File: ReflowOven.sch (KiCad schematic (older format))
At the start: 0 parts

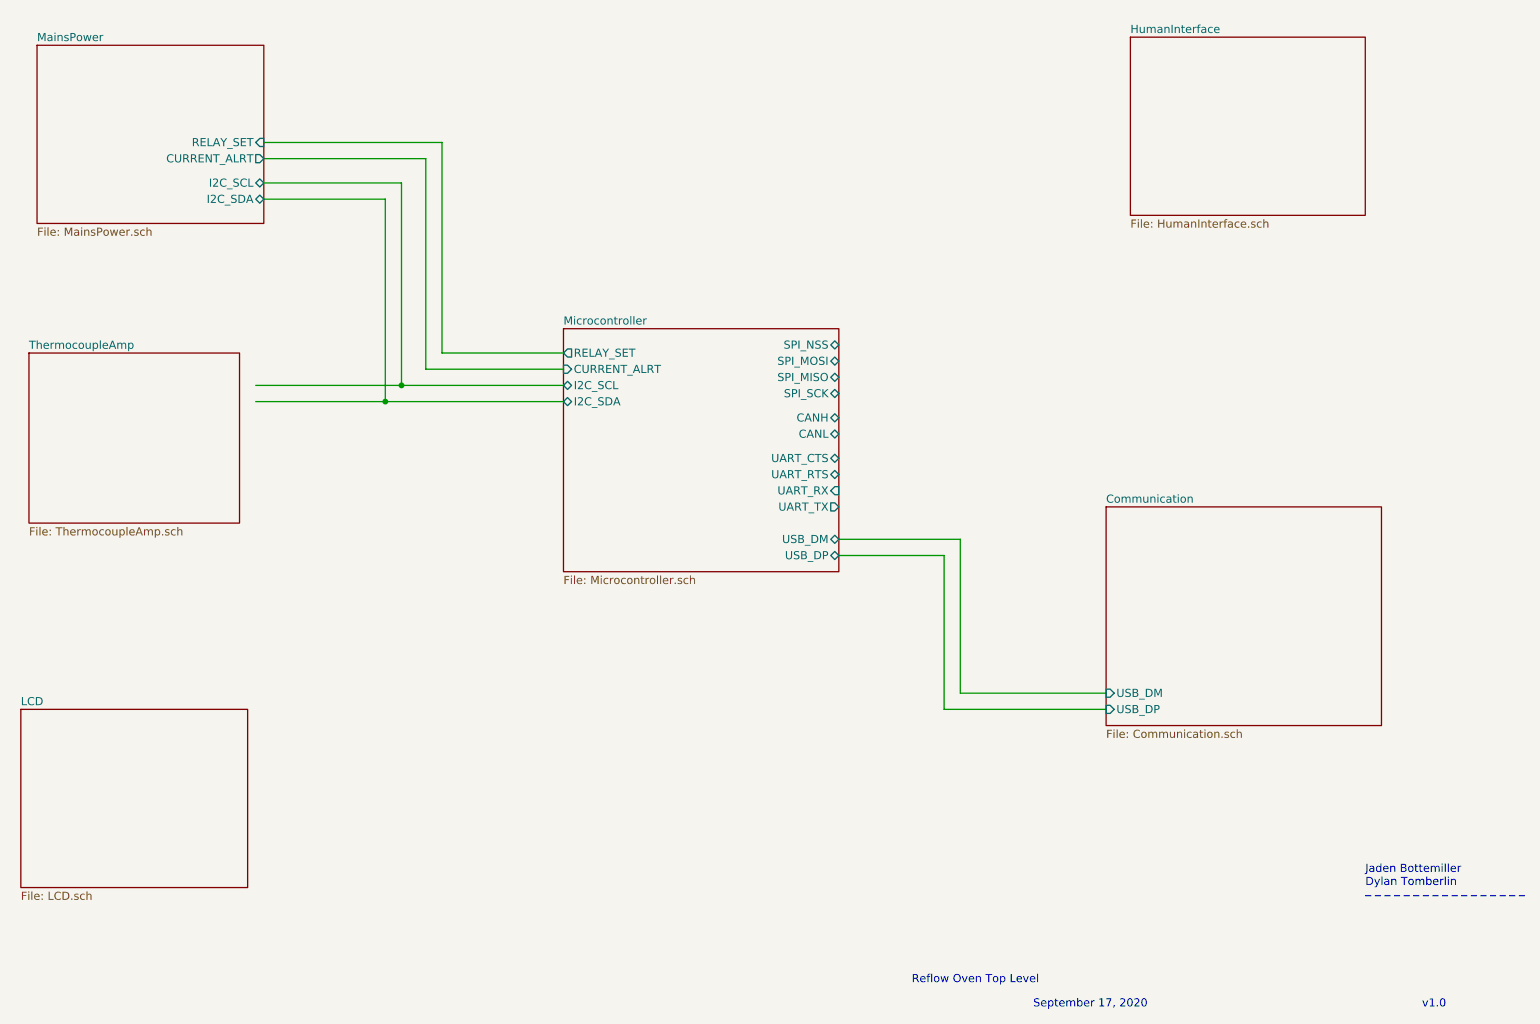
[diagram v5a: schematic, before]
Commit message: Added display driver for 7 segment
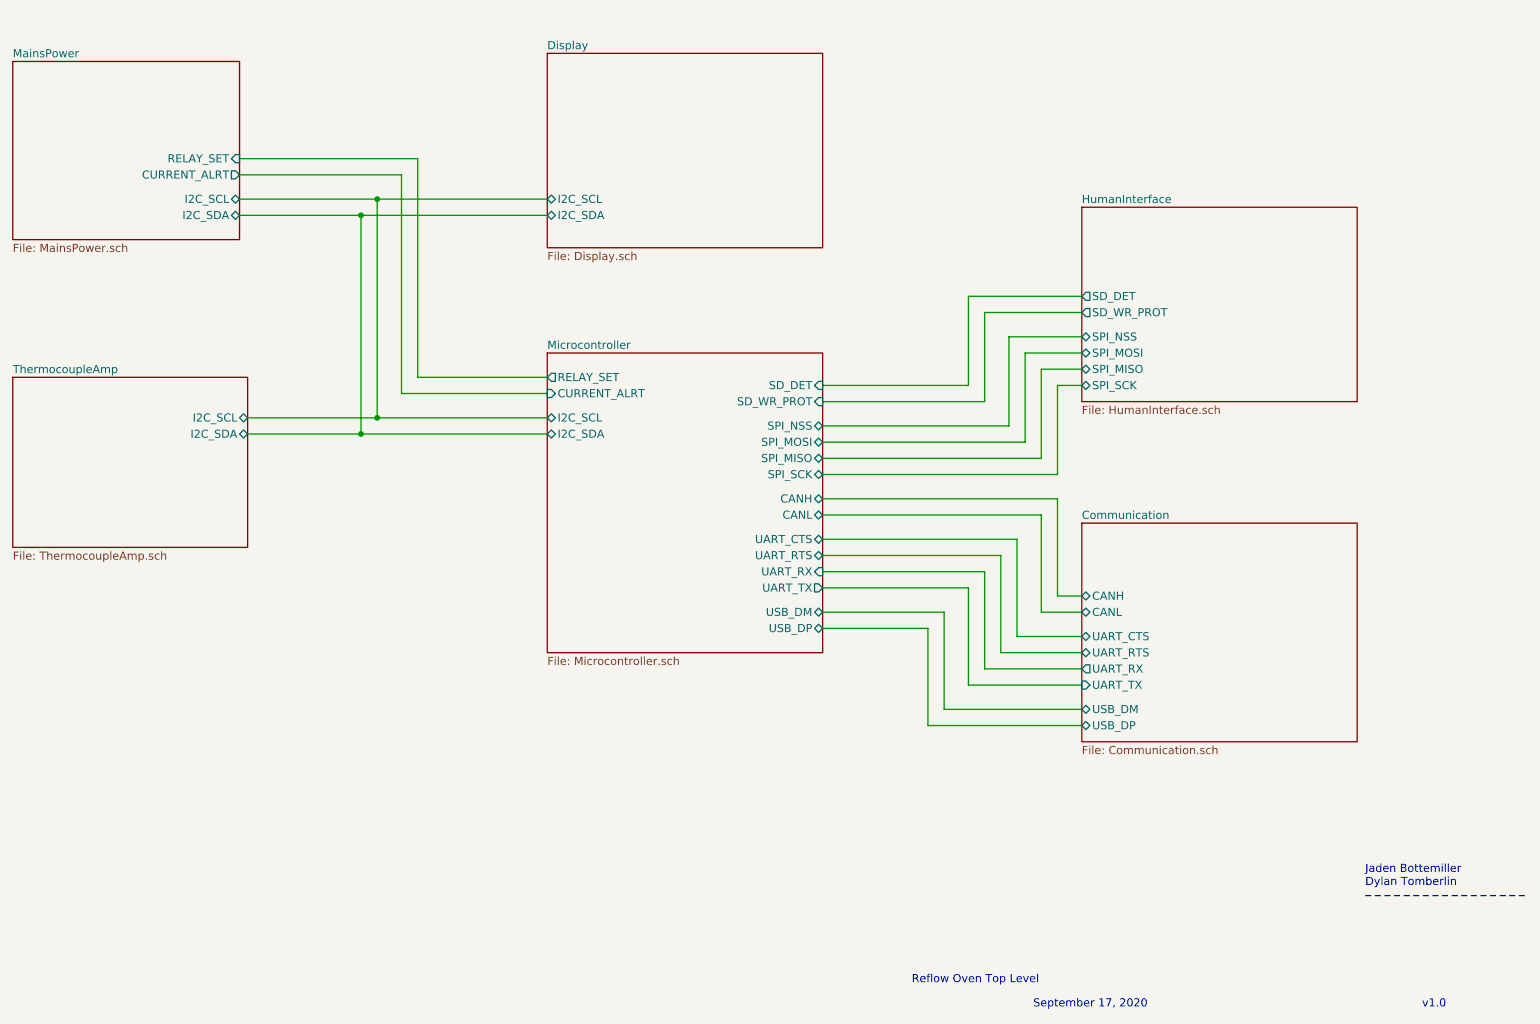
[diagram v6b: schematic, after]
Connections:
- wire segments 20 -> 58
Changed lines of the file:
@@
 	10200 6950 11200 6950
 $Sheet
-S 5250 3450 1700 1500
+S 5150 3600 1700 1850
 U 5F6415F0
 F0 "Microcontroller" 50
 F1 "Microcontroller.sch" 50
-F2 "RELAY_SET" O L 5250 3600 50
-F3 "CURRENT_ALRT" I L 5250 3700 50
-F4 "I2C_SCL" B L 5250 3800 50
-F5 "I2C_SDA" B L 5250 3900 50
-F6 "USB_DP" B R 6950 4850 50
-F7 "USB_DM" B R 6950 4750 50
-F8 "UART_TX" O R 6950 4550 50
-F9 "UART_RX" I R 6950 4450 50
-F10 "UART_RTS" B R 6950 4350 50
-F11 "UART_CTS" B R 6950 4250 50
-F12 "SPI_SCK" B R 6950 3850 50
-F13 "SPI_MISO" B R 6950 3750 50
-F14 "SPI_MOSI" B R 6950 3650 50
-F15 "SPI_NSS" B R 6950 3550 50
-F16 "CANL" B R 6950 4100 50
-F17 "CANH" B R 6950 4000 50
+F2 "RELAY_SET" O L 5150 3750 50
+F3 "CURRENT_ALRT" I L 5150 3850 50
+F4 "I2C_SCL" B L 5150 4000 50
+F5 "I2C_SDA" B L 5150 4100 50
+F6 "USB_DP" B R 6850 5300 50
+F7 "USB_DM" B R 6850 5200 50
+F8 "UART_TX" O R 6850 5050 50
+F9 "UART_RX" I R 6850 4950 50
+F10 "UART_RTS" B R 6850 4850 50
+F11 "UART_CTS" B R 6850 4750 50
+F12 "SPI_SCK" B R 6850 4350 50
+F13 "SPI_MISO" B R 6850 4250 50
+F14 "SPI_MOSI" B R 6850 4150 50
+F15 "SPI_NSS" B R 6850 4050 50
+F16 "CANL" B R 6850 4600 50
+F17 "CANH" B R 6850 4500 50
+F18 "SD_WR_PROT" I R 6850 3900 50
+F19 "SD_DET" I R 6850 3800 50
 $EndSheet
 $Sheet
-S 1900 5800 1400 1100
+S 5150 1750 1700 1200
 U 5F6416B8
-F0 "LCD" 50
-F1 "LCD.sch" 50
+F0 "Display" 50
+F1 "Display.sch" 50
+F2 "I2C_SCL" B L 5150 2650 50
+F3 "I2C_SDA" B L 5150 2750 50
 $EndSheet
 $Sheet
-S 8750 1650 1450 1100
+S 8450 2700 1700 1200
 U 5F641779
 F0 "HumanInterface" 50
 F1 "HumanInterface.sch" 50
+F2 "SPI_SCK" B L 8450 3800 50
+F3 "SPI_MISO" B L 8450 3700 50
+F4 "SPI_MOSI" B L 8450 3600 50
+F5 "SPI_NSS" B L 8450 3500 50
+F6 "SD_DET" O L 8450 3250 50
+F7 "SD_WR_PROT" O L 8450 3350 50
 $EndSheet
 $Sheet
-S 8600 4550 1700 1350
+S 8450 4650 1700 1350
 U 5F641C10
 F0 "Communication" 50
 F1 "Communication.sch" 50
-F2 "USB_DP" I L 8600 5800 50
-F3 "USB_DM" I L 8600 5700 50
+F2 "USB_DP" B L 8450 5900 50
+F3 "USB_DM" B L 8450 5800 50
+F4 "UART_TX" I L 8450 5650 50
+F5 "UART_RX" O L 8450 5550 50
+F6 "UART_RTS" B L 8450 5450 50
+F7 "UART_CTS" B L 8450 5350 50
+F8 "CANH" B L 8450 5100 50
+F9 "CANL" B L 8450 5200 50
 $EndSheet
 Wire Wire Line
-	4500 3600 4500 2300
+	4350 3750 4350 2400
 Wire Wire Line
-	4500 2300 3400 2300
+	4350 2400 3250 2400
 Wire Wire Line
-	4500 3600 5250 3600
+	4350 3750 5150 3750
 $Sheet
-S 2000 1700 1400 1100
+S 1850 1800 1400 1100
 U 5F641519
 F0 "MainsPower" 50
 F1 "MainsPower.sch" 50
-F2 "RELAY_SET" I R 3400 2300 50
-F3 "CURRENT_ALRT" O R 3400 2400 50
-F4 "I2C_SCL" B R 3400 2550 50
-F5 "I2C_SDA" B R 3400 2650 50
+F2 "RELAY_SET" I R 3250 2400 50
+F3 "CURRENT_ALRT" O R 3250 2500 50
+F4 "I2C_SCL" B R 3250 2650 50
+F5 "I2C_SDA" B R 3250 2750 50
 $EndSheet
 Wire Wire Line
-	5250 3700 4400 3700
+	5150 3850 4250 3850
 Wire Wire Line
-	4400 3700 4400 2400
+	4250 3850 4250 2500
 Wire Wire Line
-	4400 2400 3400 2400
+	4250 2500 3250 2500
 Wire Wire Line
-	3400 2550 4250 2550
+	3250 2650 4100 2650
 Wire Wire Line
-	4250 2550 4250 3800
+	4100 2650 4100 4000
 Wire Wire Line
-	4250 3800 5250 3800
+	4100 4000 5150 4000
 Wire Wire Line
-	4150 3900 4150 2650
+	4000 4100 4000 2750
 Wire Wire Line
-	4150 2650 3400 2650
+	4000 2750 3250 2750
 Wire Wire Line
-	4150 3900 5250 3900
+	4000 4100 5150 4100
 $Sheet
-S 1950 3600 1300 1050
+S 1850 3750 1450 1050
 U 5F67E1E1
 F0 "ThermocoupleAmp" 50
 F1 "ThermocoupleAmp.sch" 50
+F2 "I2C_SCL" B R 3300 4000 50
+F3 "I2C_SDA" B R 3300 4100 50
 $EndSheet
+Connection ~ 4100 4000
+Connection ~ 4000 4100
 Wire Wire Line
-	4250 3800 3350 3800
-Connection ~ 4250 3800
+	6850 5300 7500 5300
 Wire Wire Line
-	4150 3900 3350 3900
-Connection ~ 4150 3900
+	7500 5300 7500 5900
 Wire Wire Line
-	6950 4850 7600 4850
+	7500 5900 8450 5900
 Wire Wire Line
-	7600 4850 7600 5800
+	8450 5800 7600 5800
 Wire Wire Line
-	7600 5800 8600 5800
+	7600 5800 7600 5200
 Wire Wire Line
-	8600 5700 7700 5700
+	7600 5200 6850 5200
 Wire Wire Line
-	7700 5700 7700 4750
+	8450 5650 7750 5650
 Wire Wire Line
-	7700 4750 6950 4750
+	7750 5650 7750 5050
+Wire Wire Line
+	7750 5050 6850 5050
+Wire Wire Line
+	6850 4950 7850 4950
+Wire Wire Line
+	7850 4950 7850 5550
+Wire Wire Line
+	7850 5550 8450 5550
+Wire Wire Line
+	8450 5450 7950 5450
+Wire Wire Line
+	7950 5450 7950 4850
+Wire Wire Line
+	7950 4850 6850 4850
+Wire Wire Line
+	6850 4750 8050 4750
+Wire Wire Line
+	8050 4750 8050 5350
+Wire Wire Line
+	8050 5350 8450 5350
+Wire Wire Line
+	8450 5200 8200 5200
+Wire Wire Line
+	8200 5200 8200 4600
+Wire Wire Line
+	8200 4600 6850 4600
+Wire Wire Line
+	6850 4500 8300 4500
+Wire Wire Line
+	8300 4500 8300 5100
+Wire Wire Line
+	8300 5100 8450 5100
+Wire Wire Line
+	8300 4350 8300 3800
+Wire Wire Line
+	8300 3800 8450 3800
+Wire Wire Line
+	6850 4350 8300 4350
+Wire Wire Line
+	8200 3700 8200 4250
+Wire Wire Line
+	8200 4250 6850 4250
+Wire Wire Line
+	8200 3700 8450 3700
+Wire Wire Line
+	8450 3600 8100 3600
+Wire Wire Line
+	8100 3600 8100 4150
+Wire Wire Line
+	8100 4150 6850 4150
+Wire Wire Line
+	6850 4050 8000 4050
+Wire Wire Line
+	8000 4050 8000 3500
+Wire Wire Line
+	8000 3500 8450 3500
+Wire Wire Line
+	7850 3350 7850 3900
+Wire Wire Line
+	7850 3900 6850 3900
+Wire Wire Line
+	7850 3350 8450 3350
+Wire Wire Line
+	6850 3800 7750 3800
+Wire Wire Line
+	7750 3800 7750 3250
+Wire Wire Line
+	7750 3250 8450 3250
+Wire Wire Line
+	3300 4100 4000 4100
+Wire Wire Line
+	3300 4000 4100 4000
+Wire Wire Line
+	4100 2650 5150 2650
+Connection ~ 4100 2650
+Wire Wire Line
+	4000 2750 5150 2750
+Connection ~ 4000 2750
 $EndSCHEMATC

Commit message: Done with preliminary schematic. Needs review
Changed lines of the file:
@@
 	10200 6950 11200 6950
 $Sheet
-S 5150 3600 1700 1850
+S 5150 3600 1700 2100
 U 5F6415F0
 F0 "Microcontroller" 50
@@
 F4 "I2C_SCL" B L 5150 4000 50
 F5 "I2C_SDA" B L 5150 4100 50
-F6 "USB_DP" B R 6850 5300 50
-F7 "USB_DM" B R 6850 5200 50
-F8 "UART_TX" O R 6850 5050 50
-F9 "UART_RX" I R 6850 4950 50
-F10 "UART_RTS" B R 6850 4850 50
-F11 "UART_CTS" B R 6850 4750 50
-F12 "SPI_SCK" B R 6850 4350 50
-F13 "SPI_MISO" B R 6850 4250 50
-F14 "SPI_MOSI" B R 6850 4150 50
-F15 "SPI_NSS" B R 6850 4050 50
-F16 "CANL" B R 6850 4600 50
-F17 "CANH" B R 6850 4500 50
-F18 "SD_WR_PROT" I R 6850 3900 50
-F19 "SD_DET" I R 6850 3800 50
+F6 "USB_DP" B R 6850 5600 50
+F7 "USB_DM" B R 6850 5500 50
+F8 "UART_TX" O R 6850 5350 50
+F9 "UART_RX" I R 6850 5250 50
+F10 "UART_RTS" B R 6850 5150 50
+F11 "UART_CTS" B R 6850 5050 50
+F12 "SPI_SCK" B R 6850 4650 50
+F13 "SPI_MISO" B R 6850 4550 50
+F14 "SPI_MOSI" B R 6850 4450 50
+F15 "SPI_NSS" B R 6850 4350 50
+F16 "CANL" B R 6850 4900 50
+F17 "CANH" B R 6850 4800 50
+F18 "SD_WR_PROT" I R 6850 4250 50
+F19 "SD_DET" I R 6850 4150 50
+F20 "SW3" I R 6850 3800 50
+F21 "SW1" I R 6850 4000 50
+F22 "SW2" I R 6850 3900 50
 $EndSheet
 $Sheet
@@
 $EndSheet
 $Sheet
-S 8450 2700 1700 1200
+S 8450 2700 1700 1400
 U 5F641779
 F0 "HumanInterface" 50
 F1 "HumanInterface.sch" 50
-F2 "SPI_SCK" B L 8450 3800 50
-F3 "SPI_MISO" B L 8450 3700 50
-F4 "SPI_MOSI" B L 8450 3600 50
-F5 "SPI_NSS" B L 8450 3500 50
-F6 "SD_DET" O L 8450 3250 50
-F7 "SD_WR_PROT" O L 8450 3350 50
-$EndSheet
-$Sheet
-S 8450 4650 1700 1350
-U 5F641C10
-F0 "Communication" 50
-F1 "Communication.sch" 50
-F2 "USB_DP" B L 8450 5900 50
-F3 "USB_DM" B L 8450 5800 50
-F4 "UART_TX" I L 8450 5650 50
-F5 "UART_RX" O L 8450 5550 50
-F6 "UART_RTS" B L 8450 5450 50
-F7 "UART_CTS" B L 8450 5350 50
-F8 "CANH" B L 8450 5100 50
-F9 "CANL" B L 8450 5200 50
+F2 "SPI_SCK" B L 8450 4000 50
+F3 "SPI_MISO" B L 8450 3900 50
+F4 "SPI_MOSI" B L 8450 3800 50
+F5 "SPI_NSS" B L 8450 3700 50
+F6 "SD_DET" O L 8450 3450 50
+F7 "SD_WR_PROT" O L 8450 3550 50
+F8 "I2C_SCL" B L 8450 2850 50
+F9 "I2C_SDA" B L 8450 2950 50
+F10 "SW1" O L 8450 3300 50
+F11 "SW2" O L 8450 3200 50
+F12 "SW3" O L 8450 3100 50
 $EndSheet
 Wire Wire Line
@@
 	3250 2650 4100 2650
 Wire Wire Line
-	4100 2650 4100 4000
+	4100 2650 4100 3150
 Wire Wire Line
 	4100 4000 5150 4000
 Wire Wire Line
-	4000 4100 4000 2750
+	4000 4100 4000 3250
 Wire Wire Line
 	4000 2750 3250 2750
@@
 Connection ~ 4000 4100
 Wire Wire Line
-	6850 5300 7500 5300
-Wire Wire Line
-	7500 5300 7500 5900
-Wire Wire Line
-	7500 5900 8450 5900
-Wire Wire Line
-	8450 5800 7600 5800
-Wire Wire Line
-	7600 5800 7600 5200
-Wire Wire Line
-	7600 5200 6850 5200
-Wire Wire Line
-	8450 5650 7750 5650
-Wire Wire Line
-	7750 5650 7750 5050
-Wire Wire Line
-	7750 5050 6850 5050
-Wire Wire Line
-	6850 4950 7850 4950
-Wire Wire Line
-	7850 4950 7850 5550
-Wire Wire Line
-	7850 5550 8450 5550
-Wire Wire Line
-	8450 5450 7950 5450
-Wire Wire Line
-	7950 5450 7950 4850
-Wire Wire Line
-	7950 4850 6850 4850
-Wire Wire Line
-	6850 4750 8050 4750
-Wire Wire Line
-	8050 4750 8050 5350
-Wire Wire Line
-	8050 5350 8450 5350
-Wire Wire Line
-	8450 5200 8200 5200
-Wire Wire Line
-	8200 5200 8200 4600
-Wire Wire Line
-	8200 4600 6850 4600
-Wire Wire Line
-	6850 4500 8300 4500
-Wire Wire Line
-	8300 4500 8300 5100
-Wire Wire Line
-	8300 5100 8450 5100
-Wire Wire Line
-	8300 4350 8300 3800
-Wire Wire Line
-	8300 3800 8450 3800
-Wire Wire Line
-	6850 4350 8300 4350
-Wire Wire Line
-	8200 3700 8200 4250
-Wire Wire Line
-	8200 4250 6850 4250
-Wire Wire Line
-	8200 3700 8450 3700
-Wire Wire Line
-	8450 3600 8100 3600
-Wire Wire Line
-	8100 3600 8100 4150
-Wire Wire Line
-	8100 4150 6850 4150
-Wire Wire Line
-	6850 4050 8000 4050
-Wire Wire Line
-	8000 4050 8000 3500
-Wire Wire Line
-	8000 3500 8450 3500
-Wire Wire Line
-	7850 3350 7850 3900
-Wire Wire Line
-	7850 3900 6850 3900
-Wire Wire Line
-	7850 3350 8450 3350
-Wire Wire Line
-	6850 3800 7750 3800
-Wire Wire Line
-	7750 3800 7750 3250
-Wire Wire Line
-	7750 3250 8450 3250
+	8300 4650 8300 4000
+Wire Wire Line
+	8300 4000 8450 4000
+Wire Wire Line
+	6850 4650 8300 4650
+Wire Wire Line
+	8200 3900 8200 4550
+Wire Wire Line
+	8200 4550 6850 4550
+Wire Wire Line
+	8200 3900 8450 3900
+Wire Wire Line
+	8450 3800 8100 3800
+Wire Wire Line
+	8100 3800 8100 4450
+Wire Wire Line
+	8100 4450 6850 4450
+Wire Wire Line
+	6850 4350 8000 4350
+Wire Wire Line
+	8000 4350 8000 3700
+Wire Wire Line
+	8000 3700 8450 3700
+Wire Wire Line
+	7850 3550 7850 4250
+Wire Wire Line
+	7850 4250 6850 4250
+Wire Wire Line
+	7850 3550 8450 3550
+Wire Wire Line
+	6850 4150 7750 4150
+Wire Wire Line
+	7750 4150 7750 3450
+Wire Wire Line
+	7750 3450 8450 3450
 Wire Wire Line
 	3300 4100 4000 4100
@@
 	4000 2750 5150 2750
 Connection ~ 4000 2750
+Wire Wire Line
+	8450 2950 7250 2950
+Wire Wire Line
+	7250 2950 7250 3250
+Wire Wire Line
+	7250 3250 4000 3250
+Connection ~ 4000 3250
+Wire Wire Line
+	7150 3150 7150 2850
+Wire Wire Line
+	7150 2850 8450 2850
+Wire Wire Line
+	4000 2750 4000 3250
+Wire Wire Line
+	4100 3150 7150 3150
+Connection ~ 4100 3150
+Wire Wire Line
+	4100 3150 4100 4000
+Wire Wire Line
+	8450 3100 7400 3100
+Wire Wire Line
+	7400 3100 7400 3800
+Wire Wire Line
+	7400 3800 6850 3800
+Wire Wire Line
+	6850 3900 7500 3900
+Wire Wire Line
+	7500 3900 7500 3200
+Wire Wire Line
+	7500 3200 8450 3200
+Wire Wire Line
+	7600 4000 7600 3300
+Wire Wire Line
+	7600 3300 8450 3300
+Wire Wire Line
+	6850 4000 7600 4000
+Wire Wire Line
+	6850 5600 8450 5600
+Wire Wire Line
+	6850 5500 8450 5500
+Wire Wire Line
+	6850 5350 8450 5350
+Wire Wire Line
+	6850 5250 8450 5250
+Wire Wire Line
+	6850 5150 8450 5150
+Wire Wire Line
+	6850 5050 8450 5050
+Wire Wire Line
+	6850 4900 8450 4900
+Wire Wire Line
+	6850 4800 8450 4800
+$Sheet
+S 8450 4650 1700 1350
+U 5F641C10
+F0 "Communication" 50
+F1 "Communication.sch" 50
+F2 "USB_DP" B L 8450 5600 50
+F3 "USB_DM" B L 8450 5500 50
+F4 "UART_TX" I L 8450 5350 50
+F5 "UART_RX" O L 8450 5250 50
+F6 "UART_RTS" B L 8450 5150 50
+F7 "UART_CTS" B L 8450 5050 50
+F8 "CANH" B L 8450 4800 50
+F9 "CANL" B L 8450 4900 50
+$EndSheet
 $EndSCHEMATC

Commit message: Added stuff
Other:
- note added: "Designators 200+"
- note added: "Designators 300+"
- note added: "Designators 400+"
- note added: "Designators 500+"
- note added: "Designators 600+"
- note added: "Designators 700+"
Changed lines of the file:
@@
 F9 "CANL" B L 8450 4900 50
 $EndSheet
+Text Notes 5200 5650 0    50   ~ 0
+Designators 200+
+Text Notes 1900 4750 0    50   ~ 0
+Designators 600+
+Text Notes 1900 2850 0    50   ~ 0
+Designators 500+
+Text Notes 5200 2900 0    50   ~ 0
+Designators 300+
+Text Notes 9400 4050 0    50   ~ 0
+Designators 400+
+Text Notes 9400 5950 0    50   ~ 0
+Designators 700+
 $EndSCHEMATC
